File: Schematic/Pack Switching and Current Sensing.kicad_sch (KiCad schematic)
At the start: 31 parts, among them Q10 CSD19531Q5A, Q11 ZXMP10A13F, Q12 CSD19531Q5A, Q13 CSD19531Q5A, Q9 CSD19531Q5A

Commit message: added sensors?
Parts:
- removed D25: 18V, symbol Device:D_Zener_Filled
- removed Q13: CSD19531Q5A, Package_TO_SOT_SMD:TDSON-8-1, symbol Transistor_FET:CSD19531Q5A
- removed R44: 1k, symbol Device:R
- added D27: 16V, symbol Device:D_Zener_Filled
- added FB5, FB6, FB7, FB8: 220R, symbol Device:FerriteBead_Small
- added Q11, Q14, Q15, Q16, Q17: CSD19531Q5A, Package_TO_SOT_SMD:TDSON-8-1, symbol Transistor_FET:CSD19531Q5A
- added R47: 1k, symbol Device:R
- D24: value 18V -> 16V
- renumbered D26 to D25, D27 to D26, Q11 to Q13, R48 to R44, R47 to R48, R131 to R53
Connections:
- net CHG: now also FB1.1, FB3.1, FB4.1; no longer FB1.2
- net DSG: now also R54.2, D27.1 (K), FB5.2, FB6.2, FB7.2, FB8.2; no longer FB3.2, FB4.1, R54.1
- net PACK+: now also R54.1, D27.2 (A), Q14.1 (S), Q14.2 (S), Q14.3 (S), Q15.1 (S), Q15.2 (S), Q15.3 (S), Q16.1 (S), Q16.2 (S), Q16.3 (S), Q17.1 (S), Q17.2 (S), Q17.3 (S); no longer Q12.1 (S), Q12.2 (S), Q12.3 (S), R54.2
- net PCHG: now also Q10.5 (D), Q12.5 (D), Q9.5 (D), Q11.5 (D), Q14.5 (D), Q15.5 (D), Q16.5 (D), Q17.5 (D)
- net at FB4.2: now also Q12.4 (G)
- net at Q13.3 (D), R45.2, R46.2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: now also R47.2
- net at Q9.4 (G): now also FB1.2; no longer FB1.1
- net +BATT renamed BATT+
- net BATT+: now also Q12.1 (S), Q12.2 (S), Q12.3 (S), Q11.1 (S), Q11.2 (S), Q11.3 (S), R47.1
- new net: Q13.2 (S), R53.2
- new net: FB6.1, Q15.4 (G)
- new net: FB5.1, Q14.4 (G)
- new net: FB7.1, Q16.4 (G)
- new net: FB8.1, Q17.4 (G)
- new net: FB3.2, Q11.4 (G)
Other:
- note added: ">2W resistors"
- note removed: "5W resistors"
- moved on the sheet: C19, C20, C21, C22, D23, D24, D25, D26, E1, FB1, NT1, Q13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

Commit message: 1st Schematic Review
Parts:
- renumbered C19 to C22, C20 to C23, C21 to C24, C22 to C25, R44 to R46, R45 to R47, R46 to R48, R47 to R49, R48 to R50, R49 to R51, R50 to R52, R51 to R53, R52 to R54, R53 to R55, R54 to R56
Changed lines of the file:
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@@
 	)
 	(junction
-		(at 129.54 147.32)
-		(diameter 0)
-		(color 0 0 0 0)
-	)
-	(junction
 		(at 135.89 140.97)
 		(diameter 0)
@@
 	(wire
 		(pts
-			(xy 129.54 147.32) (xy 129.54 146.05)
+			(xy 129.54 146.05) (xy 129.54 148.59)
 		)
 		(stroke
@@
 	(wire
 		(pts
-			(xy 129.54 148.59) (xy 129.54 147.32)
-		)
-		(stroke
-			(width 0)
-			(type default)
-		)
-	)
-	(wire
-		(pts
 			(xy 135.89 74.93) (xy 135.89 72.39)
 		)
@@
 		(on_board yes)
 		(dnp no)
-		(property "Reference" "R49"
+		(property "Reference" "R51"
 			(at 138.684 134.62 90)
 			(effects
@@
 			(project "STAR"
 				(path "/fc8533bc-25dd-4c20-9b4c-ffebebd6739b/e8da5d81-614b-4fe5-84b3-4c351fab7114/cc0a7e05-dd91-401b-a994-41ee02720f37"
-					(reference "R49")
+					(reference "R51")
 					(unit 1)
 				)
@@
 		(on_board yes)
 		(dnp no)
-		(property "Reference" "R53"
+		(property "Reference" "R55"
 			(at 153.924 104.394 0)
 			(effects
@@
 			(project "STAR"
 				(path "/fc8533bc-25dd-4c20-9b4c-ffebebd6739b/e8da5d81-614b-4fe5-84b3-4c351fab7114/cc0a7e05-dd91-401b-a994-41ee02720f37"
-					(reference "R53")
+					(reference "R55")
 					(unit 1)
 				)
@@
 		(on_board yes)
 		(dnp no)
-		(property "Reference" "R44"
+		(property "Reference" "R46"
 			(at 108.458 40.894 90)
 			(effects
@@
 			(project "STAR"
 				(path "/fc8533bc-25dd-4c20-9b4c-ffebebd6739b/e8da5d81-614b-4fe5-84b3-4c351fab7114/cc0a7e05-dd91-401b-a994-41ee02720f37"
-					(reference "R44")
+					(reference "R46")
 					(unit 1)
 				)
@@
 		(on_board yes)
 		(dnp no)
-		(property "Reference" "R51"
+		(property "Reference" "R53"
 			(at 138.684 139.7 90)
 			(effects
@@
 			(project "STAR"
 				(path "/fc8533bc-25dd-4c20-9b4c-ffebebd6739b/e8da5d81-614b-4fe5-84b3-4c351fab7114/cc0a7e05-dd91-401b-a994-41ee02720f37"
-					(reference "R51")
+					(reference "R53")
 					(unit 1)
 				)
@@
 		(on_board yes)
 		(dnp no)
-		(property "Reference" "C22"
+		(property "Reference" "C25"
 			(at 210.82 134.112 0)
 			(effects
@@
 			(project "STAR"
 				(path "/fc8533bc-25dd-4c20-9b4c-ffebebd6739b/e8da5d81-614b-4fe5-84b3-4c351fab7114/cc0a7e05-dd91-401b-a994-41ee02720f37"
-					(reference "C22")
+					(reference "C25")
 					(unit 1)
 				)
@@
 		(on_board yes)
 		(dnp no)
-		(property "Reference" "R46"
+		(property "Reference" "R48"
 			(at 124.714 107.95 90)
 			(effects
@@
 			(project "STAR"
 				(path "/fc8533bc-25dd-4c20-9b4c-ffebebd6739b/e8da5d81-614b-4fe5-84b3-4c351fab7114/cc0a7e05-dd91-401b-a994-41ee02720f37"
-					(reference "R46")
+					(reference "R48")
 					(unit 1)
 				)
@@
 		(on_board yes)
 		(dnp no)
-		(property "Reference" "R54"
+		(property "Reference" "R56"
 			(at 196.088 40.894 90)
 			(effects
@@
 			(project "STAR"
 				(path "/fc8533bc-25dd-4c20-9b4c-ffebebd6739b/e8da5d81-614b-4fe5-84b3-4c351fab7114/cc0a7e05-dd91-401b-a994-41ee02720f37"
-					(reference "R54")
+					(reference "R56")
 					(unit 1)
 				)
@@
 		(on_board yes)
 		(dnp no)
-		(property "Reference" "#PWR017"
+		(property "Reference" "#PWR022"
 			(at 129.54 154.94 0)
 			(effects
@@
 			(project "STAR"
 				(path "/fc8533bc-25dd-4c20-9b4c-ffebebd6739b/e8da5d81-614b-4fe5-84b3-4c351fab7114/cc0a7e05-dd91-401b-a994-41ee02720f37"
-					(reference "#PWR017")
+					(reference "#PWR022")
 					(unit 1)
 				)
@@
 		(on_board yes)
 		(dnp no)
-		(property "Reference" "R47"
+		(property "Reference" "R49"
 			(at 124.714 110.49 90)
 			(effects
@@
 			(project "STAR"
 				(path "/fc8533bc-25dd-4c20-9b4c-ffebebd6739b/e8da5d81-614b-4fe5-84b3-4c351fab7114/cc0a7e05-dd91-401b-a994-41ee02720f37"
-					(reference "R47")
+					(reference "R49")
 					(unit 1)
 				)
@@
 		(on_board yes)
 		(dnp no)
-		(property "Reference" "R48"
+		(property "Reference" "R50"
 			(at 124.714 113.03 90)
 			(effects
@@
 			(project "STAR"
 				(path "/fc8533bc-25dd-4c20-9b4c-ffebebd6739b/e8da5d81-614b-4fe5-84b3-4c351fab7114/cc0a7e05-dd91-401b-a994-41ee02720f37"
-					(reference "R48")
+					(reference "R50")
 					(unit 1)
 				)
@@
 		(on_board yes)
 		(dnp no)
-		(property "Reference" "R52"
+		(property "Reference" "R54"
 			(at 138.684 142.24 90)
 			(effects
@@
 			(project "STAR"
 				(path "/fc8533bc-25dd-4c20-9b4c-ffebebd6739b/e8da5d81-614b-4fe5-84b3-4c351fab7114/cc0a7e05-dd91-401b-a994-41ee02720f37"
-					(reference "R52")
+					(reference "R54")
 					(unit 1)
 				)
@@
 		(on_board yes)
 		(dnp no)
-		(property "Reference" "C20"
+		(property "Reference" "C23"
 			(at 148.59 122.174 90)
 			(effects
@@
 			(project "STAR"
 				(path "/fc8533bc-25dd-4c20-9b4c-ffebebd6739b/e8da5d81-614b-4fe5-84b3-4c351fab7114/cc0a7e05-dd91-401b-a994-41ee02720f37"
-					(reference "C20")
+					(reference "C23")
 					(unit 1)
 				)
@@
 		(on_board yes)
 		(dnp no)
-		(property "Reference" "R50"
+		(property "Reference" "R52"
 			(at 138.684 137.16 90)
 			(effects
@@
 			(project "STAR"
 				(path "/fc8533bc-25dd-4c20-9b4c-ffebebd6739b/e8da5d81-614b-4fe5-84b3-4c351fab7114/cc0a7e05-dd91-401b-a994-41ee02720f37"
-					(reference "R50")
+					(reference "R52")
 					(unit 1)
 				)
@@
 		(on_board yes)
 		(dnp no)
-		(property "Reference" "R45"
+		(property "Reference" "R47"
 			(at 124.714 105.41 90)
 			(effects
@@
 			(project "STAR"
 				(path "/fc8533bc-25dd-4c20-9b4c-ffebebd6739b/e8da5d81-614b-4fe5-84b3-4c351fab7114/cc0a7e05-dd91-401b-a994-41ee02720f37"
-					(reference "R45")
+					(reference "R47")
 					(unit 1)
 				)
@@
 		(on_board yes)
 		(dnp no)
-		(property "Reference" "#PWR016"
+		(property "Reference" "#PWR021"
 			(at 102.87 138.43 0)
 			(effects
@@
 			(project "STAR"
 				(path "/fc8533bc-25dd-4c20-9b4c-ffebebd6739b/e8da5d81-614b-4fe5-84b3-4c351fab7114/cc0a7e05-dd91-401b-a994-41ee02720f37"
-					(reference "#PWR016")
+					(reference "#PWR021")
 					(unit 1)
 				)
@@
 		(on_board yes)
 		(dnp no)
-		(property "Reference" "C19"
+		(property "Reference" "C22"
 			(at 134.62 122.174 90)
 			(effects
@@
 			(project "STAR"
 				(path "/fc8533bc-25dd-4c20-9b4c-ffebebd6739b/e8da5d81-614b-4fe5-84b3-4c351fab7114/cc0a7e05-dd91-401b-a994-41ee02720f37"
-					(reference "C19")
-					(unit 1)
-				)
-			)
-		)
-	)
-	(symbol
-		(lib_id "PCM_4ms_Power-symbol:PWR_FLAG")
-		(at 129.54 147.32 270)
-		(unit 1)
-		(exclude_from_sim no)
-		(in_bom yes)
-		(on_board yes)
-		(dnp no)
-		(property "Reference" "#FLG03"
-			(at 131.445 147.32 0)
-			(effects
-				(font
-					(size 1.27 1.27)
-				)
-				(hide yes)
-			)
-		)
-		(property "Value" "PWR_FLAG"
-			(at 132.08 147.32 90)
-			(effects
-				(font
-					(size 1.27 1.27)
-				)
-				(justify left)
-			)
-		)
-		(property "Footprint" ""
-			(at 129.54 147.32 0)
-			(effects
-				(font
-					(size 1.27 1.27)
-				)
-				(hide yes)
-			)
-		)
-		(property "Datasheet" ""
-			(at 129.54 147.32 0)
-			(effects
-				(font
-					(size 1.27 1.27)
-				)
-				(hide yes)
-			)
-		)
-		(property "Description" ""
-			(at 129.54 147.32 0)
-			(effects
-				(font
-					(size 1.27 1.27)
-				)
-				(hide yes)
-			)
-		)
-		(pin "1"
-		)
-		(instances
-			(project "STAR"
-				(path "/fc8533bc-25dd-4c20-9b4c-ffebebd6739b/e8da5d81-614b-4fe5-84b3-4c351fab7114/cc0a7e05-dd91-401b-a994-41ee02720f37"
-					(reference "#FLG03")
+					(reference "C22")
 					(unit 1)
 				)
@@
 		(on_board yes)
 		(dnp no)
-		(property "Reference" "C21"
+		(property "Reference" "C24"
 			(at 210.82 126.492 0)
 			(effects
@@
 			(project "STAR"
 				(path "/fc8533bc-25dd-4c20-9b4c-ffebebd6739b/e8da5d81-614b-4fe5-84b3-4c351fab7114/cc0a7e05-dd91-401b-a994-41ee02720f37"
-					(reference "C21")
+					(reference "C24")
 					(unit 1)
 				)

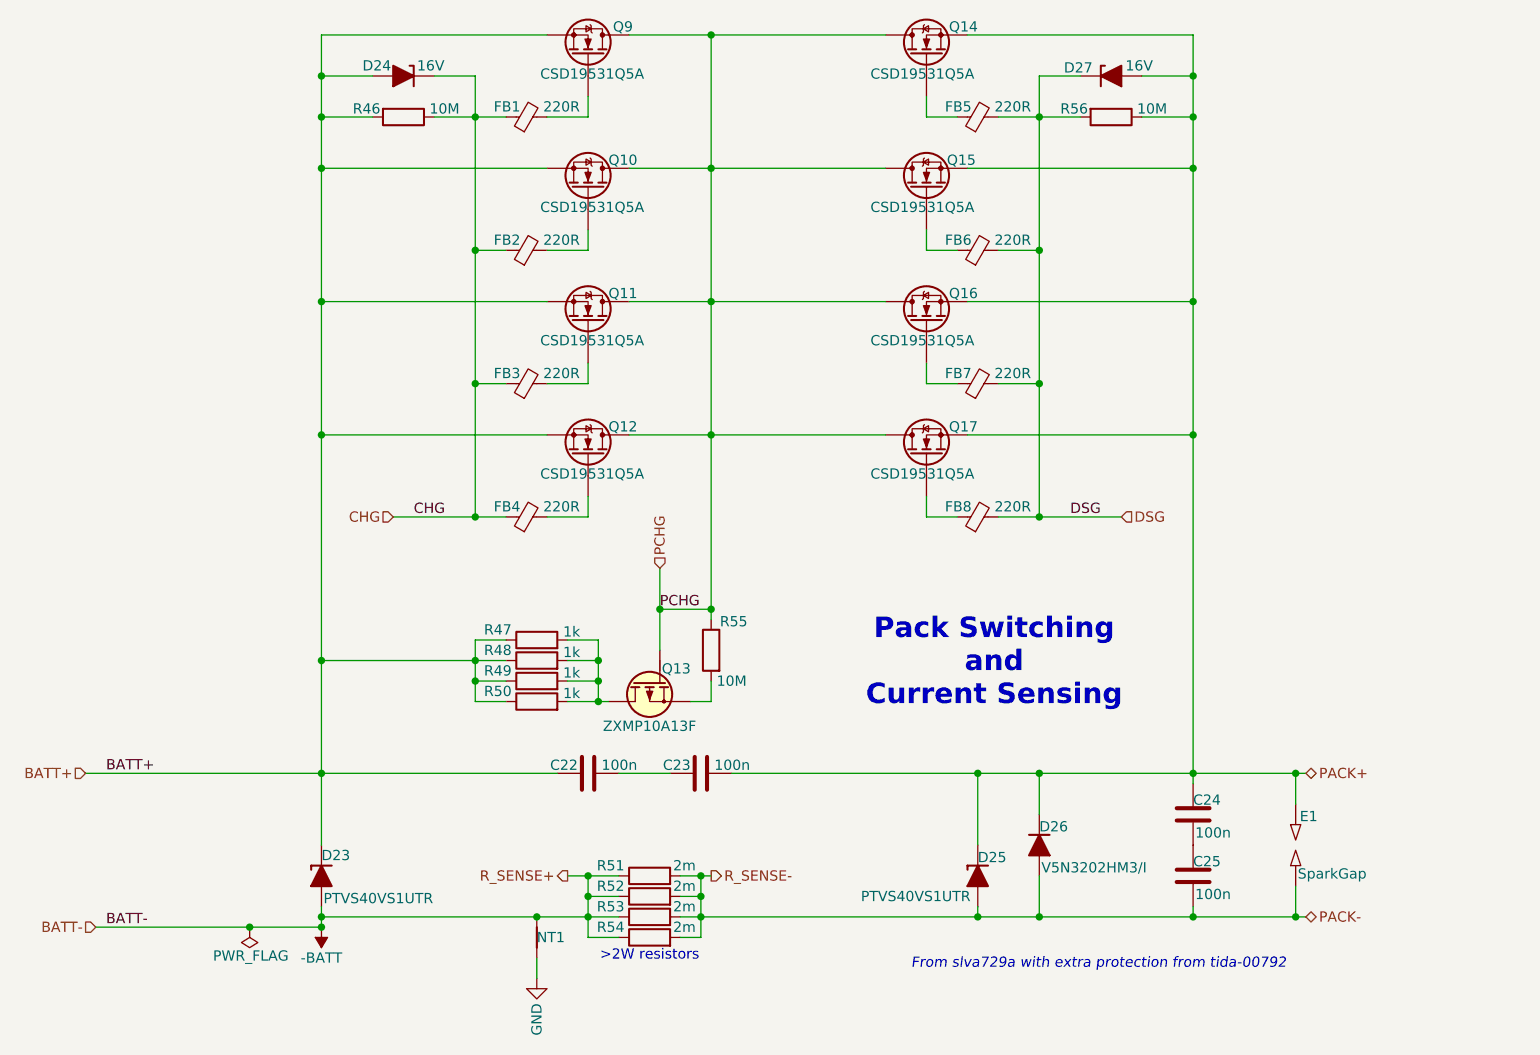
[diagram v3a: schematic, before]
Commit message: Added MCU
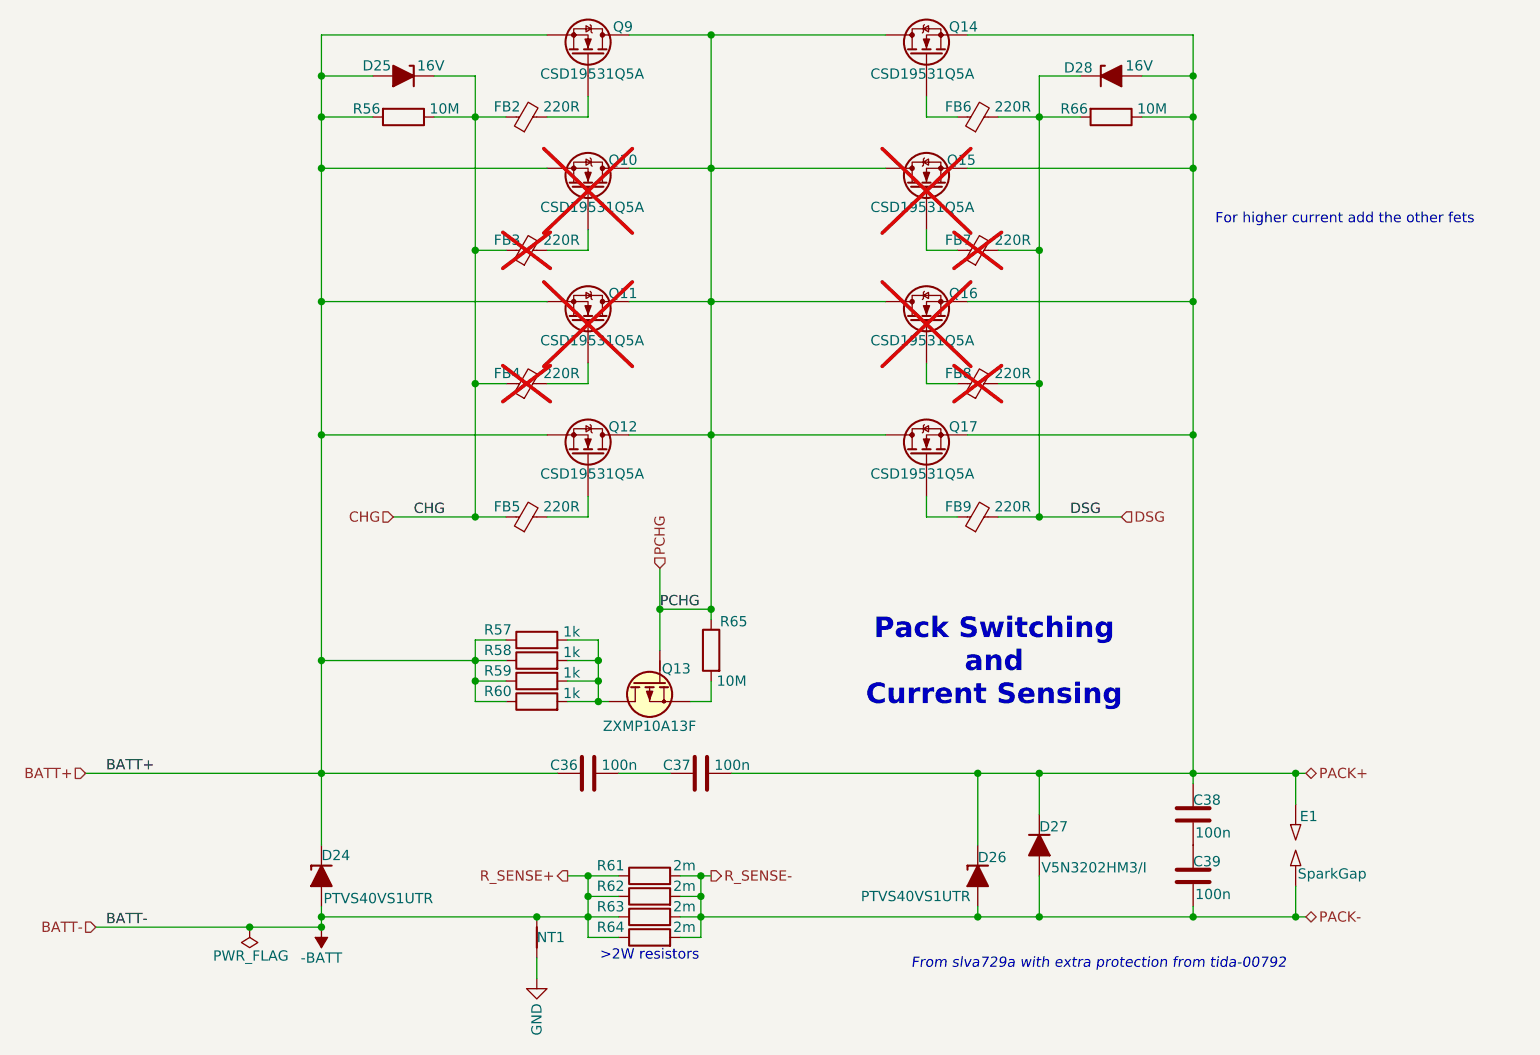
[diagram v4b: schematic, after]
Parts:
- FB3: renamed from FB2; now not fitted
- FB4: renamed from FB3; now not fitted
- FB7: renamed from FB6; now not fitted
- FB8: renamed from FB7; now not fitted
- Q10, Q11, Q15, Q16: now not fitted
- renumbered C22 to C36, C23 to C37, C24 to C38, C25 to C39, D23 to D24, D24 to D25, D25 to D26, D26 to D27, D27 to D28, FB1 to FB2, FB4 to FB5, FB5 to FB6, FB8 to FB9, R46 to R56, R47 to R57, R48 to R58, R49 to R59, R50 to R60, R51 to R61, R52 to R62, R53 to R63, R54 to R64, R55 to R65, R56 to R66
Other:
- note added: "For higher current add the other fets"

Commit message: Started to work on the BOM
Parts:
- removed D27: V5N3202HM3/I, symbol Device:D_Filled
- added D24: V5N3202HM3/I, V5N3202HM3-I:DFN33A_VIS, symbol V5N3202HM3-I:V5N3202HM3_I
- C31: renamed from C36; footprint (none) -> Capacitor_SMD:C_1206_3216Metric_Pad1.33x1.80mm_HandSolder; Link (none) -> https://mou.sr/4n9ybmQ; Manufacturer Part Number (none) -> CL31B104KBCNNNC; Price per Unit (none) -> 0.11; Supplier (none) -> Mouser; Supplier Part Number (none) -> 187-CL31B104KBCNNNC
- C32: renamed from C37; footprint (none) -> Capacitor_SMD:C_1206_3216Metric_Pad1.33x1.80mm_HandSolder; Link (none) -> https://mou.sr/4n9ybmQ; Manufacturer Part Number (none) -> CL31B104KBCNNNC; Price per Unit (none) -> 0.11; Supplier (none) -> Mouser; Supplier Part Number (none) -> 187-CL31B104KBCNNNC
- C33: renamed from C38; footprint (none) -> Capacitor_SMD:C_1206_3216Metric_Pad1.33x1.80mm_HandSolder; Link (none) -> https://mou.sr/4n9ybmQ; Manufacturer Part Number (none) -> CL31B104KBCNNNC; Price per Unit (none) -> 0.11; Supplier (none) -> Mouser; Supplier Part Number (none) -> 187-CL31B104KBCNNNC
- C34: renamed from C39; footprint (none) -> Capacitor_SMD:C_1206_3216Metric_Pad1.33x1.80mm_HandSolder; Link (none) -> https://mou.sr/4n9ybmQ; Manufacturer Part Number (none) -> CL31B104KBCNNNC; Price per Unit (none) -> 0.11; Supplier (none) -> Mouser; Supplier Part Number (none) -> 187-CL31B104KBCNNNC
- D21: renamed from D24; footprint PCM_Diode_SMD_AKL:D_SOD-123F -> PTVS40VS1UTR,115:SOD123W; Link (none) -> https://mou.sr/3VlU6vr; Manufacturer Part Number (none) -> PTVS40VS1UTR,115; Price per Unit (none) -> 0.42; Supplier (none) -> Mouser; Supplier Part Number (none) -> 771-PTVS40VS1UTR115771-PTVS40VS1UTR115
- D22: renamed from D25; footprint (none) -> MMSZ3V9T1G:SOD3716X135N; Link (none) -> https://mou.sr/42anHLN; Manufacturer Part Number (none) -> MMSZ5246B-TP; Price per Unit (none) -> 0.10; Supplier (none) -> Mouser; Supplier Part Number (none) -> 833-MMSZ5246B-TP
- D23: renamed from D26; footprint PCM_Diode_SMD_AKL:D_SOD-123F -> PTVS40VS1UTR,115:SOD123W; Link (none) -> https://mou.sr/3VlU6vr; Manufacturer Part Number (none) -> PTVS40VS1UTR,115; Price per Unit (none) -> 0.42; Supplier (none) -> Mouser; Supplier Part Number (none) -> 771-PTVS40VS1UTR115771-PTVS40VS1UTR115
- D25: renamed from D28; footprint (none) -> MMSZ3V9T1G:SOD3716X135N; Link (none) -> https://mou.sr/42anHLN; Manufacturer Part Number (none) -> MMSZ5246B-TP; Price per Unit (none) -> 0.10; Supplier (none) -> Mouser; Supplier Part Number (none) -> 833-MMSZ5246B-TP
- E1: now left out of the parts list
- Q10, Q11, Q12, Q14, Q15, Q16, Q17, Q9: footprint Package_TO_SOT_SMD:TDSON-8-1 -> (none)
- Q13: footprint PCM_Package_TO_SOT_SMD_AKL:SOT-23 -> (none)
- renumbered R56 to R52, R57 to R53, R58 to R54, R59 to R55, R60 to R56, R61 to R57, R62 to R58, R63 to R59, R64 to R60, R65 to R61, R66 to R62
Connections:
- net PACK+: now also D24.5, D24.6, D24.7, D24.8
- net PACK-: now also D24.1, D24.2, D24.3, D24.4
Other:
- moved on the sheet: C33, C34, D21, D23

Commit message: Massive pivit, simplification
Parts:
- renumbered C31 to C24, C32 to C25, C33 to C26, C34 to C27, D21 to D20, D22 to D21, D23 to D22, D24 to D23, D25 to D24, FB2 to FB1, FB3 to FB2, FB4 to FB3, FB5 to FB4, FB6 to FB5, FB7 to FB6, FB8 to FB7, FB9 to FB8
